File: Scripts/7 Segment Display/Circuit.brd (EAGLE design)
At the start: 68.6 x 53.3 mm, 4 parts

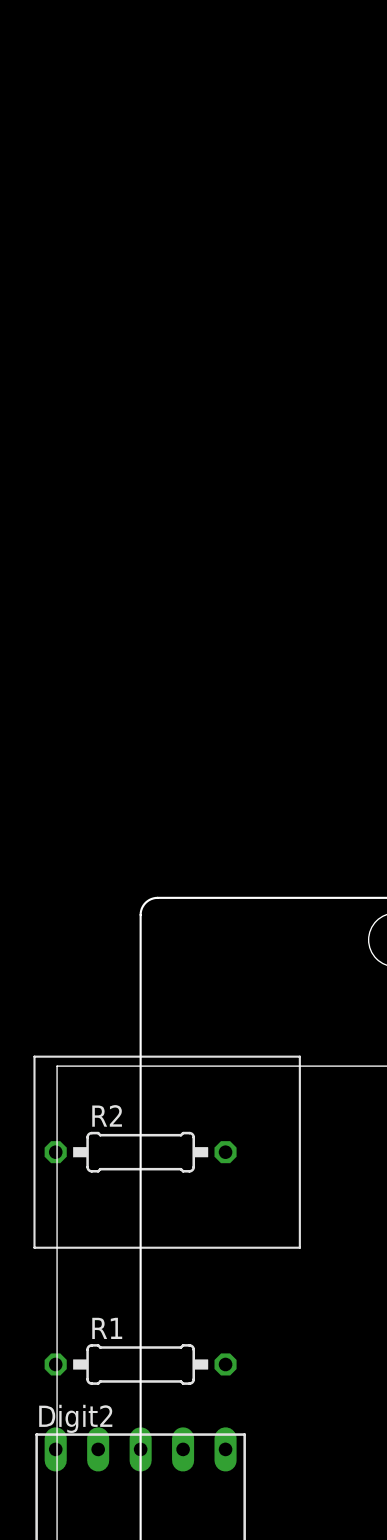
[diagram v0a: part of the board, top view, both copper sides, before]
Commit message: Improved the code for 7 segments display script
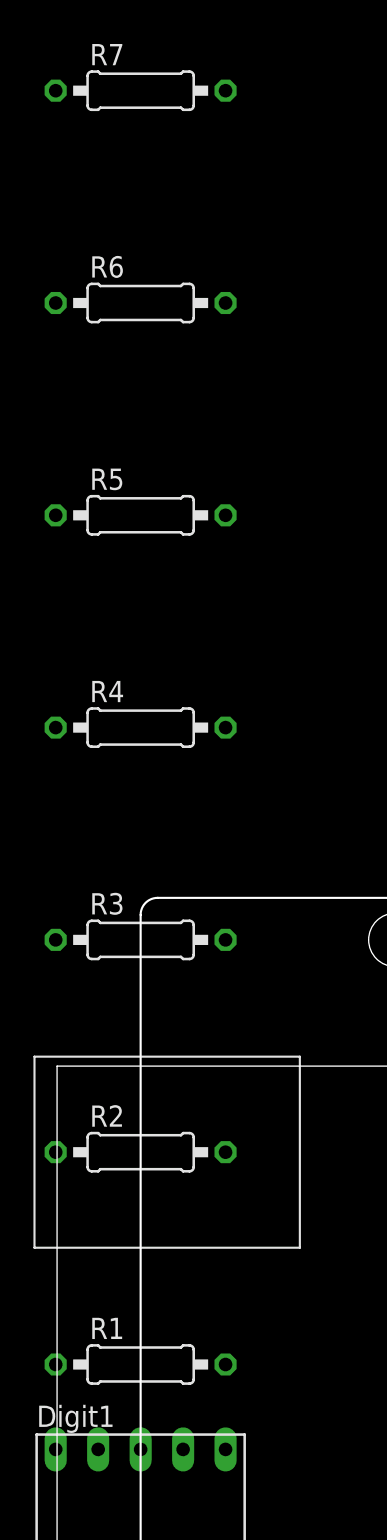
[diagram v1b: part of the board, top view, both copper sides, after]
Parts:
- added R3, R4, R5, R6, R7: 1k‎Ω, AUTODESK_CIRCUITS_BREADBOARD:0207/10
- R1, R2: value 1kâ€ŽÎ© -> 1k‎Ω
- renumbered Digit2 to Digit1
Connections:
- new net N$13: Digit1.9, R6.2
- new net N$14: R6.1, U1.7
- new net N$15: Digit1.10, R7.2
- new net N$16: R7.1, U1.8
- net N$1: now also Digit1.8, U1.GND; no longer Digit1.7, U1.11
- net N$10: now also R4.1, U1.2; no longer R2.1, U1.GND.
- net N$11: now also Digit1.6, R5.2; no longer Digit1.8, R1.2
- net N$12: now also R5.1, U1.3; no longer Digit1.3, R2.2
- net N$2: now also Digit1.3, U1.GND.; no longer Digit1.1, U1.9
- net N$3: now also R1.1; no longer U1.7
- net N$4: now also Digit1.2, R2.1; no longer Digit1.9, U1.12
- net N$5: now also R1.2, U1.4; no longer Digit1.10, U1.13
- net N$6: now also R2.2, U1.5; no longer Digit1.2, U1.8
- net N$7: now also R3.2; no longer Digit1.5
- net N$8: now also Digit1.1, R3.1; no longer Digit1.6, U1.10
- net N$9: now also Digit1.7, R4.2; no longer R1.1, U1.GND..
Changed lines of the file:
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@@
 <description language="de">&lt;b&gt;EAGLE Design Rules&lt;/b&gt;';
 &lt;p&gt;';
-Die Standard-Design-Rules sind so gewÃ¤hlt, dass sie fÃ¼r ';
+Die Standard-Design-Rules sind so gewählt, dass sie für ';
 die meisten Anwendungen passen. Sollte ihre Platine ';
 besondere Anforderungen haben, treffen Sie die erforderlichen';
@@
 </autorouter>
 <elements>
-<element value="" name="U1" library="AUTODESK_CIRCUITS_BREADBOARD" package="ARDUINO_UNO" x="5" y="10.08"></element><element value="" name="Digit2" library="AUTODESK_CIRCUITS_BREADBOARD" package="HDSP-M" x="5" y="22.78"></element><element value="1kâ€ŽÎ©" name="R1" library="AUTODESK_CIRCUITS_BREADBOARD" package="0207/10" x="5" y="35.480000000000004"></element><element value="1kâ€ŽÎ©" name="R2" library="AUTODESK_CIRCUITS_BREADBOARD" package="0207/10" x="5" y="48.18"></element></elements>
+<element value="" name="U1" library="AUTODESK_CIRCUITS_BREADBOARD" package="ARDUINO_UNO" x="5" y="10.08"></element><element value="" name="Digit1" library="AUTODESK_CIRCUITS_BREADBOARD" package="HDSP-M" x="5" y="22.78"></element><element value="1k‎Ω" name="R1" library="AUTODESK_CIRCUITS_BREADBOARD" package="0207/10" x="5" y="35.480000000000004"></element><element value="1k‎Ω" name="R2" library="AUTODESK_CIRCUITS_BREADBOARD" package="0207/10" x="5" y="48.18"></element><element value="1k‎Ω" name="R3" library="AUTODESK_CIRCUITS_BREADBOARD" package="0207/10" x="5" y="60.879999999999995"></element><element value="1k‎Ω" name="R4" library="AUTODESK_CIRCUITS_BREADBOARD" package="0207/10" x="5" y="73.58"></element><element value="1k‎Ω" name="R5" library="AUTODESK_CIRCUITS_BREADBOARD" package="0207/10" x="5" y="86.28"></element><element value="1k‎Ω" name="R6" library="AUTODESK_CIRCUITS_BREADBOARD" package="0207/10" x="5" y="98.98"></element><element value="1k‎Ω" name="R7" library="AUTODESK_CIRCUITS_BREADBOARD" package="0207/10" x="5" y="111.68"></element></elements>
 <signals>
-<signal name="N$1"><contactref element="Digit2" pad="7"></contactref><contactref element="U1" pad="11"></contactref><wire x1="7.54" y1="30.400000000000002" x2="39.036" y2="60.879999999999995" width="0" layer="19" extent="1-1"></wire></signal><signal name="N$2"><contactref element="Digit2" pad="1"></contactref><contactref element="U1" pad="9"></contactref><wire x1="-0.08000000000000007" y1="15.16" x2="44.116" y2="60.879999999999995" width="0" layer="19" extent="1-1"></wire></signal><signal name="N$3"><contactref element="Digit2" pad="4"></contactref><contactref element="U1" pad="7"></contactref><wire x1="7.54" y1="15.16" x2="50.72" y2="60.879999999999995" width="0" layer="19" extent="1-1"></wire></signal><signal name="N$4"><contactref element="Digit2" pad="9"></contactref><contactref element="U1" pad="12"></contactref><wire x1="2.46" y1="30.400000000000002" x2="36.495999999999995" y2="60.879999999999995" width="0" layer="19" extent="1-1"></wire></signal><signal name="N$5"><contactref element="Digit2" pad="10"></contactref><contactref element="U1" pad="13"></contactref><wire x1="-0.08000000000000007" y1="30.400000000000002" x2="33.956" y2="60.879999999999995" width="0" layer="19" extent="1-1"></wire></signal><signal name="N$6"><contactref element="Digit2" pad="2"></contactref><contactref element="U1" pad="8"></contactref><wire x1="2.46" y1="15.16" x2="46.656" y2="60.879999999999995" width="0" layer="19" extent="1-1"></wire></signal><signal name="N$7"><contactref element="Digit2" pad="5"></contactref><contactref element="U1" pad="6"></contactref><wire x1="10.08" y1="15.16" x2="53.26" y2="60.879999999999995" width="0" layer="19" extent="1-1"></wire></signal><signal name="N$8"><contactref element="Digit2" pad="6"></contactref><contactref element="U1" pad="10"></contactref><wire x1="10.08" y1="30.400000000000002" x2="41.576" y2="60.879999999999995" width="0" layer="19" extent="1-1"></wire></signal><signal name="N$9"><contactref element="U1" pad="GND.."></contactref><contactref element="R1" pad="1"></contactref><wire x1="45.64" y1="12.620000000000001" x2="-0.08000000000000007" y2="35.480000000000004" width="0" layer="19" extent="1-1"></wire></signal><signal name="N$10"><contactref element="U1" pad="GND."></contactref><contactref element="R2" pad="1"></contactref><wire x1="48.18" y1="12.620000000000001" x2="-0.08000000000000007" y2="48.18" width="0" layer="19" extent="1-1"></wire></signal><signal name="N$11"><contactref element="R1" pad="2"></contactref><contactref element="Digit2" pad="8"></contactref><wire x1="10.08" y1="35.480000000000004" x2="5" y2="30.400000000000002" width="0" layer="19" extent="1-1"></wire></signal><signal name="N$12"><contactref element="R2" pad="2"></contactref><contactref element="Digit2" pad="3"></contactref><wire x1="10.08" y1="48.18" x2="5" y2="15.16" width="0" layer="19" extent="1-1"></wire></signal></signals>
+<signal name="N$1"><contactref element="U1" pad="GND"></contactref><contactref element="Digit1" pad="8"></contactref><wire x1="31.416" y1="60.879999999999995" x2="5" y2="30.400000000000002" width="0" layer="19" extent="1-1"></wire></signal><signal name="N$2"><contactref element="Digit1" pad="3"></contactref><contactref element="U1" pad="GND."></contactref><wire x1="5" y1="15.16" x2="48.18" y2="12.620000000000001" width="0" layer="19" extent="1-1"></wire></signal><signal name="N$3"><contactref element="Digit1" pad="4"></contactref><contactref element="R1" pad="1"></contactref><wire x1="7.54" y1="15.16" x2="-0.08000000000000007" y2="35.480000000000004" width="0" layer="19" extent="1-1"></wire></signal><signal name="N$4"><contactref element="Digit1" pad="2"></contactref><contactref element="R2" pad="1"></contactref><wire x1="2.46" y1="15.16" x2="-0.08000000000000007" y2="48.18" width="0" layer="19" extent="1-1"></wire></signal><signal name="N$5"><contactref element="R1" pad="2"></contactref><contactref element="U1" pad="4"></contactref><wire x1="10.08" y1="35.480000000000004" x2="58.34" y2="60.879999999999995" width="0" layer="19" extent="1-1"></wire></signal><signal name="N$6"><contactref element="R2" pad="2"></contactref><contactref element="U1" pad="5"></contactref><wire x1="10.08" y1="48.18" x2="55.8" y2="60.879999999999995" width="0" layer="19" extent="1-1"></wire></signal><signal name="N$7"><contactref element="R3" pad="2"></contactref><contactref element="U1" pad="6"></contactref><wire x1="10.08" y1="60.879999999999995" x2="53.26" y2="60.879999999999995" width="0" layer="19" extent="1-1"></wire></signal><signal name="N$8"><contactref element="R3" pad="1"></contactref><contactref element="Digit1" pad="1"></contactref><wire x1="-0.08000000000000007" y1="60.879999999999995" x2="-0.08000000000000007" y2="15.16" width="0" layer="19" extent="1-1"></wire></signal><signal name="N$9"><contactref element="R4" pad="2"></contactref><contactref element="Digit1" pad="7"></contactref><wire x1="10.08" y1="73.58" x2="7.54" y2="30.400000000000002" width="0" layer="19" extent="1-1"></wire></signal><signal name="N$10"><contactref element="R4" pad="1"></contactref><contactref element="U1" pad="2"></contactref><wire x1="-0.08000000000000007" y1="73.58" x2="63.42" y2="60.879999999999995" width="0" layer="19" extent="1-1"></wire></signal><signal name="N$11"><contactref element="R5" pad="2"></contactref><contactref element="Digit1" pad="6"></contactref><wire x1="10.08" y1="86.28" x2="10.08" y2="30.400000000000002" width="0" layer="19" extent="1-1"></wire></signal><signal name="N$12"><contactref element="R5" pad="1"></contactref><contactref element="U1" pad="3"></contactref><wire x1="-0.08000000000000007" y1="86.28" x2="60.88" y2="60.879999999999995" width="0" layer="19" extent="1-1"></wire></signal><signal name="N$13"><contactref element="R6" pad="2"></contactref><contactref element="Digit1" pad="9"></contactref><wire x1="10.08" y1="98.98" x2="2.46" y2="30.400000000000002" width="0" layer="19" extent="1-1"></wire></signal><signal name="N$14"><contactref element="R6" pad="1"></contactref><contactref element="U1" pad="7"></contactref><wire x1="-0.08000000000000007" y1="98.98" x2="50.72" y2="60.879999999999995" width="0" layer="19" extent="1-1"></wire></signal><signal name="N$15"><contactref element="R7" pad="2"></contactref><contactref element="Digit1" pad="10"></contactref><wire x1="10.08" y1="111.68" x2="-0.08000000000000007" y2="30.400000000000002" width="0" layer="19" extent="1-1"></wire></signal><signal name="N$16"><contactref element="R7" pad="1"></contactref><contactref element="U1" pad="8"></contactref><wire x1="-0.08000000000000007" y1="111.68" x2="46.656" y2="60.879999999999995" width="0" layer="19" extent="1-1"></wire></signal></signals>
 </board>
 </drawing>
